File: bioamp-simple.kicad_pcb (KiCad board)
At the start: 2 copper layers, 70 x 50 mm, 29 parts, among them J1 Conn_01x05, J2 Conn_01x02, J3 Conn_01x03, J4 POT, U1 TL074

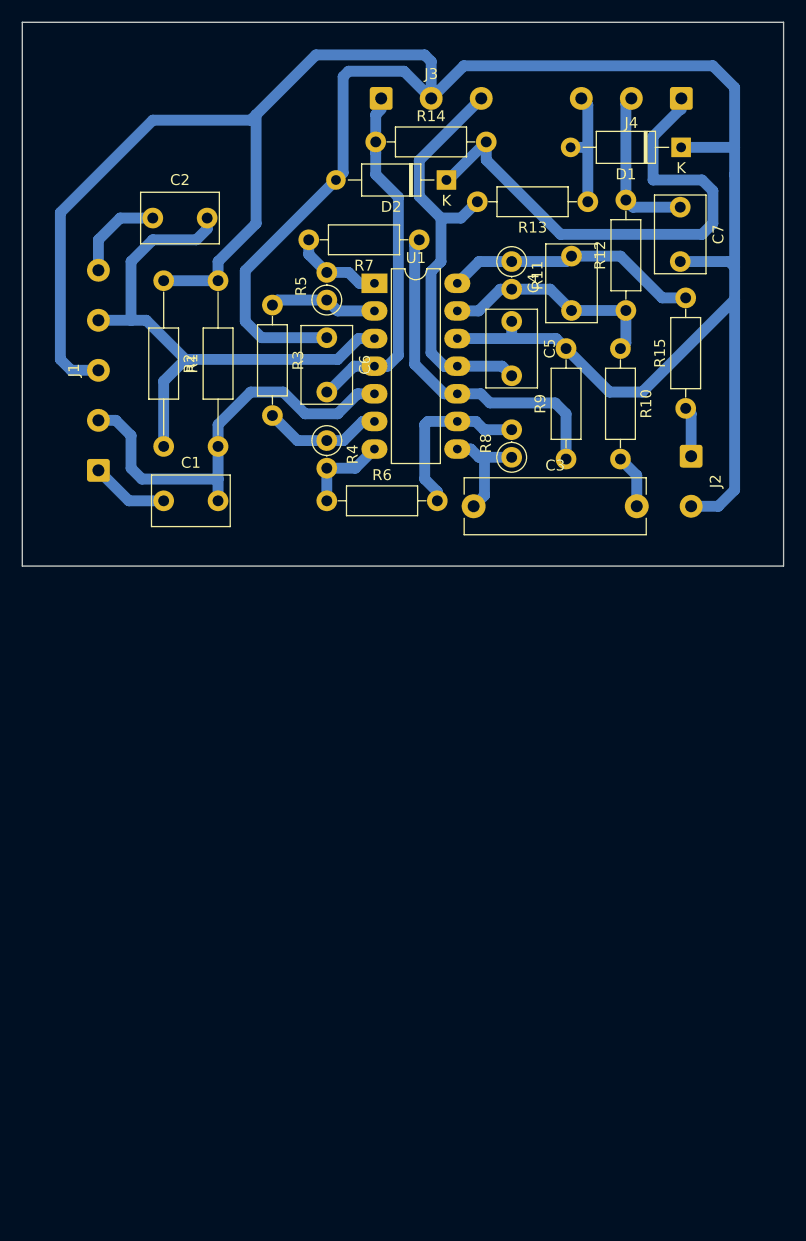
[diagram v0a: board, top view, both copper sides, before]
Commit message: earth zone added
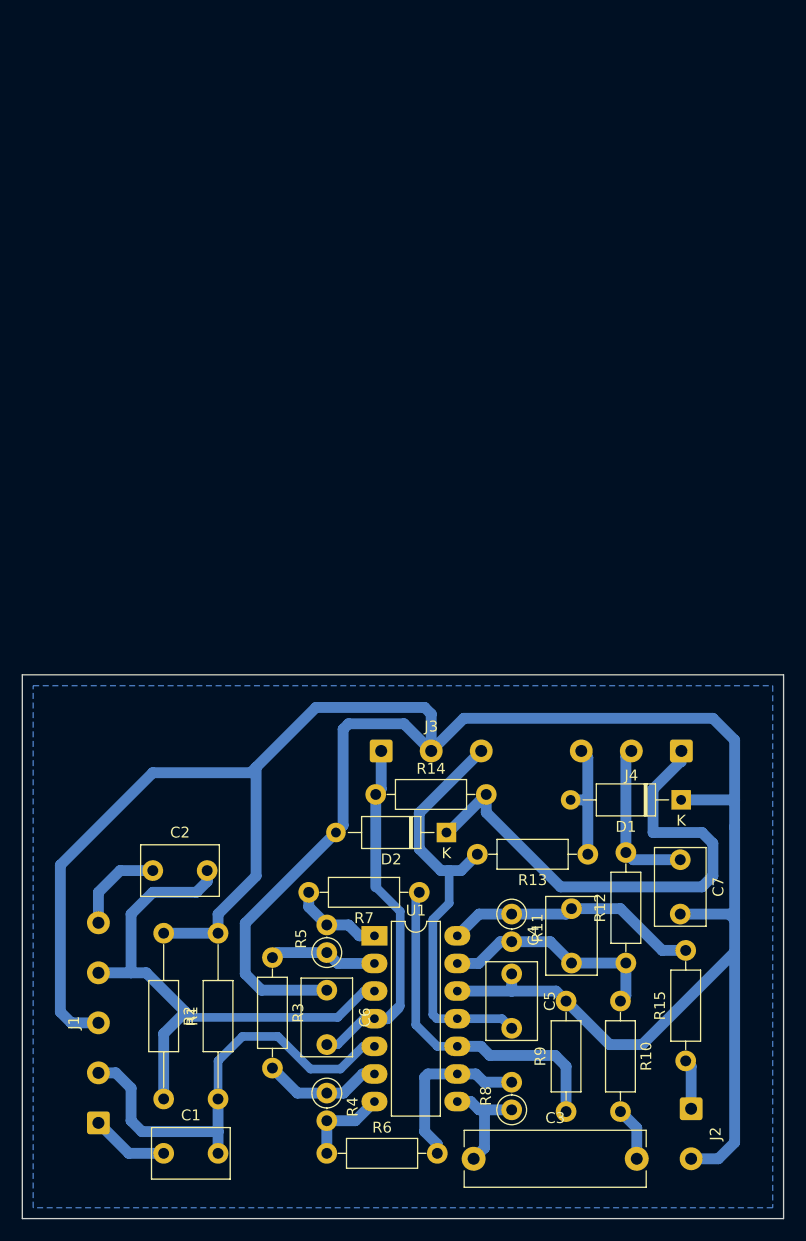
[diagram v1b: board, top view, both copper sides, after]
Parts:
- moved J2 60.0 mm to (156.5, 114.9)
- moved R2 60.0 mm to (108.0, 98.8)
- moved R5 60.0 mm to (123.0, 100.5)
- moved C1 60.0 mm to (108.0, 119.0)
- moved C2 60.0 mm to (107.0, 93.0)
- moved C3 60.0 mm to (136.5, 119.5)
- moved C4 60.0 mm to (145.5, 101.5)
- moved C5 60.0 mm to (140.0, 102.5)
- moved C6 60.0 mm to (123.0, 104.0)
- moved C7 60.0 mm to (155.5, 92.0)
- moved D1 60.0 mm to (155.6, 86.5)
- moved D2 60.0 mm to (134.0, 89.5)
- moved J1 60.0 mm to (102.0, 116.2)
- moved J3 60.0 mm to (128.0, 82.0)
- moved J4 60.0 mm to (155.6, 82.0)
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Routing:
- net Net-(J1-Pin_2): track 39.2 -> 40.9 mm
- net +6V: track 31.7 -> 32.8 mm
- net -6V: track 40.4 -> 39.8 mm
- added copper zone on B.Cu, net GND
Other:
- board text added: "Зона, соединённая с {dblquote}землёй{dblquote} залита для тех, кто фрезерует платы. Для ЛУТ её лучше удалить."
